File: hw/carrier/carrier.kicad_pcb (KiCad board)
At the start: 2 copper layers, 70 x 50 mm, 51 parts, among them J10 TP4056 IN- / mount, J2 PCM5102A I2S, J3 PCM5102A analog, J4 MAX4466 pigtail, J5 TP4056 OUT-/B-, J6 TP4056 B+/OUT+, J7 debug TX, J8 LiPo JST-PH, J9 TP4056 IN+ / mount (J6b), Q1 DMG3415U, Q2 BC557, SW1 power SPDT 1A, SW2 MODE 6x6, U1 TL431A, X1 scope X RCA pads, Y1 scope Y RCA pads

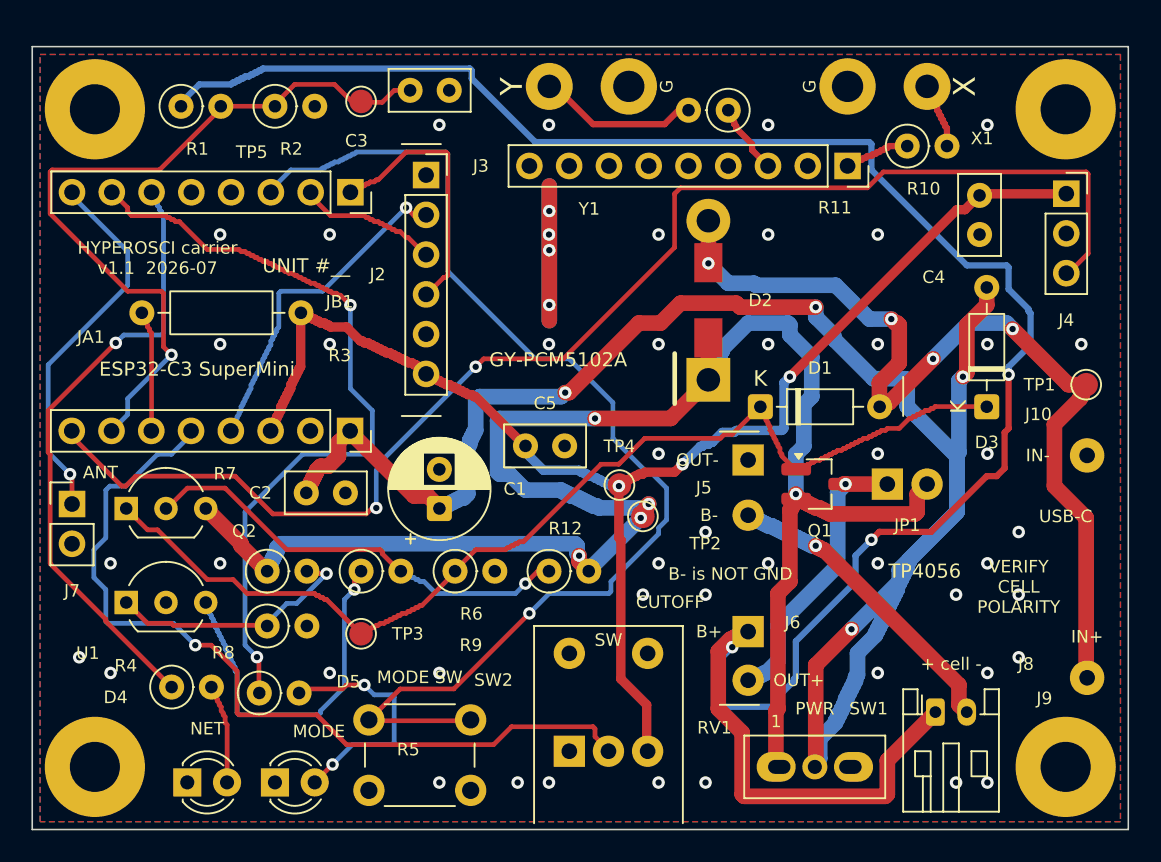
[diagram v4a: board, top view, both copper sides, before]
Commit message: hw/carrier: WIP pre-fab DFM pass — board is UNROUTED, do not plot gerbers
Implements the v1.1 pre-fab fix list. Everything that does not depend on
routing is done and passes; the router seed re-sweep is not, so the board is
committed straight out of gen_board.py with 58 unconnected items.

A1 — silk stroke 0.12 -> 0.15 mm (JLC minimum; all 70 items were under spec).
One constant, SILK_W, replaces seven literals. Height stays 0.8 mm: raising it
would grow every bounding box on a board whose placement search cannot absorb
that. 282 stock-footprint outlines are still at 0.12 and are left alone —
they are graphic lines, not text, and JLC's floor is about legibility.

A2 — SW1's plated slots re-cut to a 2x aspect: 1.80 x 0.90 drill at +/-2.45,
was 1.44 x 0.90 (1.6x). The plan's pad size (2.9 x 1.9) was NOT adopted: it
leaves 0.20 mm to the centre pad and produced four clearance violations against
the 0.25 mm netclass. Keeping the pad at 2.5 x 1.9 gives a 0.40 mm gap and a
0.35 mm long-axis annular ring.

A3 — silk legends no longer print under a fitted module. The three module
bodies were computed and then never added to `occupied`, so six strings —
including all four battery-polarity legends — were being placed where a seated
module hides them. Bodies are now a shadow list with a per-placement exemption
(a pad's own legend may sit under the module that covers that pad).

Two defects the plan did not name, both found while fixing A3:

  - find_spot's whole-board sweep had no distance bound, so a string that could
    not fit near its anchor was placed anywhere it fit. On the shipped board
    that had already scattered VERIFY CELL POLARITY 34 mm from the thing it
    warns about. Bounded to SCAN_REACH = 12 mm.
  - designators were placed in dict order, so early ones took spots the last
    ones needed. Now most-constrained-first, re-ranked after every placement.

Closing the shadow cost 18 unplaced strings; the path back to 0 was the two
fixes above, an own-courtyard fal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
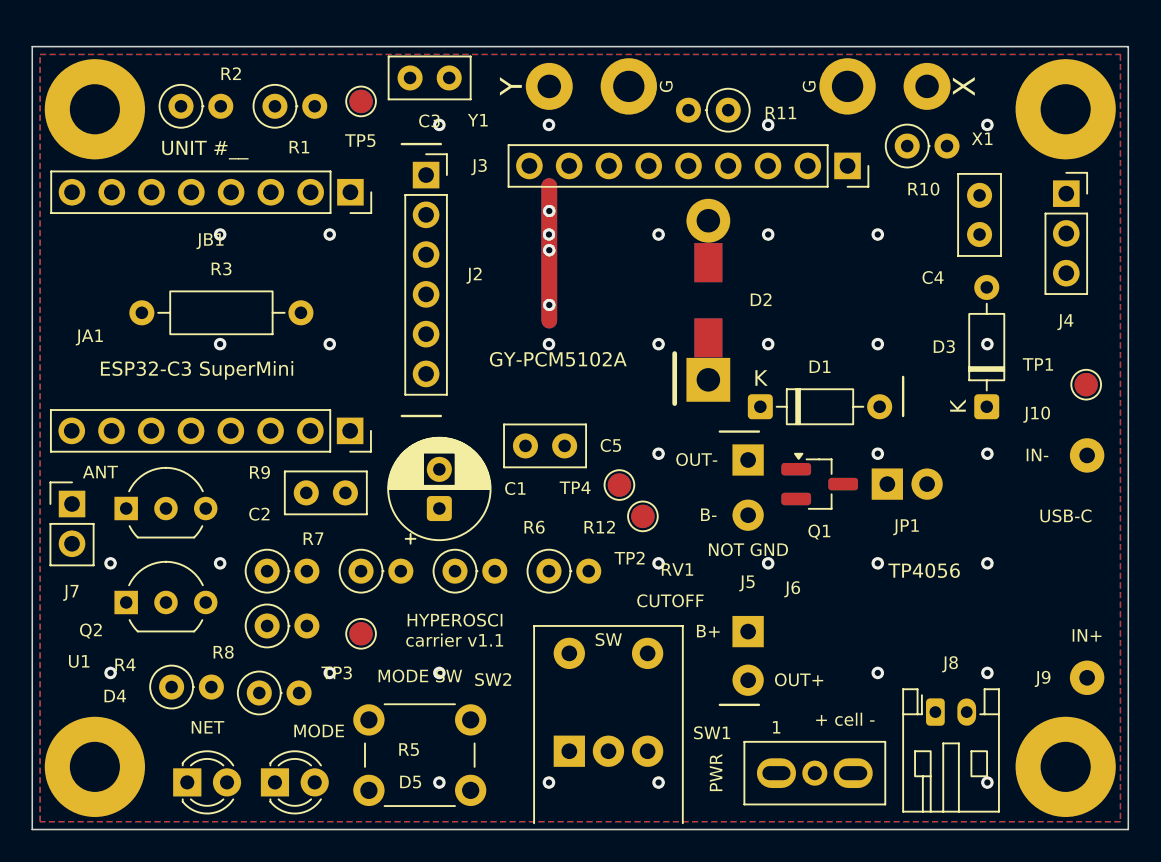
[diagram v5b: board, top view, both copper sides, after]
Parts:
- moved C3 0.79 mm to (24.1, 2.00)
- moved SW1 0.40 mm to (50.0, 46.4)
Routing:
- net BAT_PLUS: track 134.5 -> 0.00 mm, vias 3 -> 0
- net VLOAD: track 118.9 -> 0.00 mm, vias 4 -> 0
- net VSW: track 113.4 -> 0.00 mm, vias 5 -> 0
- net 3V3: track 88.9 -> 0.00 mm, vias 3 -> 0
- net MIC_OUT: track 87.5 -> 0.00 mm, vias 2 -> 0
- net BTN_MODE: track 74.5 -> 0.00 mm, vias 1 -> 0
- net GATE: track 68.6 -> 0.00 mm
- net VBUS_CHG: track 59.0 -> 0.00 mm, vias 4 -> 0
- net POT_WIPER: track 54.6 -> 0.00 mm, vias 1 -> 0
- net LED_MODE_A: track 50.0 -> 0.00 mm, vias 2 -> 0
- net VBAT_SENSE: track 48.7 -> 0.00 mm, vias 1 -> 0
- net LED_NET_A: track 39.7 -> 0.00 mm, vias 1 -> 0
- net Q2_B: track 28.5 -> 0.00 mm, vias 1 -> 0
- net DBG_TX: track 24.1 -> 0.00 mm, vias 1 -> 0
- net TL431_K: track 23.3 -> 0.00 mm, vias 1 -> 0
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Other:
- board text added: "HYPEROSCI carrier v1.1"
- board text added: "NOT GND"
- board text removed: "B- is NOT GND"
- board text removed: "HYPEROSCI carrier v1.1 2026-07"
- board text removed: "VERIFY CELL POLARITY"

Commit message: hw/carrier: routed on seed 33 — the board is fabbable again
Completes the WIP pre-fab pass. c48cff9 left carrier.kicad_pcb straight out of
gen_board.py with 58 unconnected items because the DFM fixes moved copper and
invalidated the router seed. They are now routed, every gate passes, and the
width tables are regenerated from the routed copper instead of from memory.

Seed 11 is dead. Three sub-millimetre moves killed it — SW1's slot pads out to
+/-2.45, SW1 itself 0.4 mm south, C3 0.79 mm north — and it came back 1
unconnected / 1 unrouted on BAT_PLUS. Worth stating plainly: 11 had held through
two previous re-routes and was not a fragile choice. A 16-variant sweep (4 seeds
x 4 halo settings, 32 threads, 1277 s wall) returned EXACTLY ONE clean result:
halo-off / seed 33. Every other variant lost a net, and the whole seed-20260726
family ended phase D STUCK with a severed GND_main — the failure mode a stale
seed produces instead of an error.

Adopted by rebuilding from source rather than promoting the scratch board, three
times, all landing on 1343 segments / 48 GND vias / 0 failures, pour whole at
phase D round 0 with zero repair vias.

The halo env vars did NOT need adopting: route.py gates the whole halo behind
`if HALO_COST > 0` and the repo default cost is 0, so the sweep's "halo-off" is
behaviourally identical to the repo default. Seed 33 reproduces from
ROUTE_SEED=33 alone — one line, not three.

Gates: DRC 0 violations / 0 unconnected; parity 69, unchanged from the pre-route
baseline (the documented benign 60+9); check_netlist OK; audit_board all five;
silk 0 items below 0.15 mm; drill T4=0.900 with both SW1 slots plotting 0.90 mm
of travel (X47.08->X47.98, X51.98->X52.88), which is the JLC 2x-aspect fix
verified where it actually matters.

VSW and VLOAD swapped roles, and the docs said the wrong one for two re-routes.
Every previous version of the 6.4 table called VLOAD the problem (91 mm at
0.3 mm, 152 mohm). On seed 33 VLOAD is 1.0 mm over its whole 82.6 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
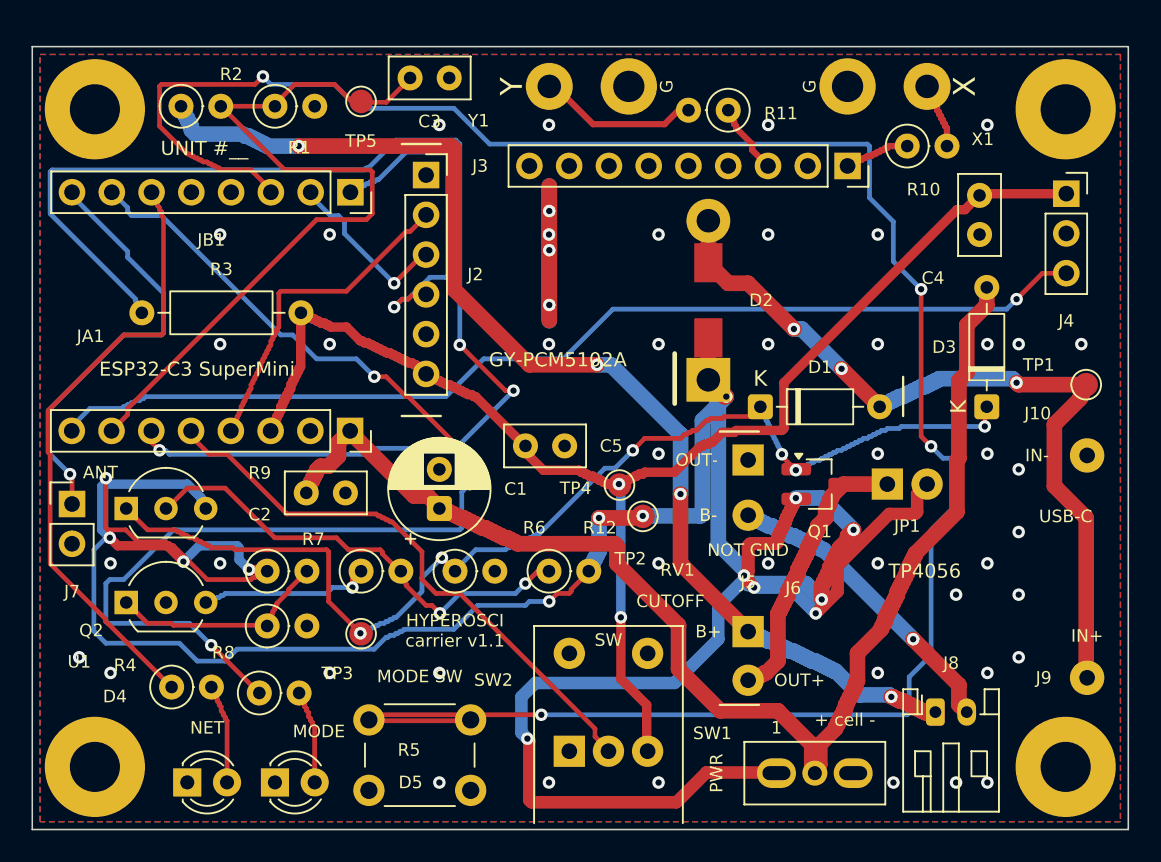
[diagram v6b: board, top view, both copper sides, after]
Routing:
- net VSW: track 0.00 -> 209.3 mm, vias 0 -> 15
- net BTN_MODE: track 0.00 -> 140.0 mm, vias 0 -> 4
- net 3V3: track 0.00 -> 88.7 mm, vias 0 -> 2
- net VLOAD: track 0.00 -> 82.6 mm
- net GPIO2_PU: track 0.00 -> 81.9 mm, vias 0 -> 3
- net BAT_PLUS: track 0.00 -> 74.8 mm, vias 0 -> 4
- net LED_MODE_A: track 0.00 -> 73.0 mm, vias 0 -> 3
- net GATE: track 0.00 -> 72.6 mm, vias 0 -> 6
- net MIC_OUT: track 0.00 -> 67.8 mm, vias 0 -> 1
- net VBUS_CHG: track 0.00 -> 51.5 mm, vias 0 -> 3
- net VBAT_SENSE: track 0.00 -> 50.4 mm
- net LED_NET_A: track 0.00 -> 39.7 mm
- net POT_WIPER: track 0.00 -> 36.7 mm
- net Q2_B: track 0.00 -> 29.8 mm, vias 0 -> 2
- net DBG_TX: track 0.00 -> 27.5 mm, vias 0 -> 1
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
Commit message: hw/carrier: back-silk artwork — 48 mark + ponkiePCBv1 wordmark
The back silkscreen carried 2 items against the front's 374, and the fab prints
that layer whether or not anything is on it, so the space was already bought.

Placement was searched rather than eyeballed: the largest pad-clear rectangle on
B.Cu is 14.5 x 15.0 mm at (26.8, 9.2). The mark takes the top 10.4 mm at its
traced 1.393 aspect and the wordmark sits in the 4.6 mm underneath, so the two
read as one lockup. Worth recording that the two windows found during the search
— a 14.8 x 15.2 block and a 22 x 4 "via-free banner" — came from independent
searches and OVERLAP, so only one could hold artwork; that is why the wordmark
went under the mark instead of into a strip of its own.

No copper moved, and that was verified rather than asserted: regenerating with
the artwork in place re-routed to the same 1343 segments / 48 vias / 0 failures,
phase D single cluster at round 0, and measure_copper returned identical widths
on every net. Silk cannot invalidate ROUTE_SEED.

Board-level graphics, not a footprint, deliberately. A footprint with no
schematic symbol is an extra_footprint under --schematic-parity, which would
have moved a baseline documented as 69 and read by diffing — for a decoration.
Parity stayed at exactly 69 (60 + 9).

tools/gen_artwork.py does the tracing. bitmap2component was not usable: it is
GUI-only, does nothing under xvfb, and emits an opaque .kicad_mod that nothing
in this repo could regenerate. potrace instead, with -a 0 -n so the output is
polygons rather than Beziers. Two details that are not obvious:

  - KiCad graphics have no polygon-with-holes primitive, so holes are keyholed
    into the exterior as a zero-width slit. Without it the two counters of the
    8 fill in solid. At silk resolution the slit is invisible.
  - Back-layer graphics are stored in top-view coordinates, so back_art()
    mirrors in X. Without that the mark reads backwards on the physical board,
    and the edi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
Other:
- board text added: "ponkiePCBv1"
